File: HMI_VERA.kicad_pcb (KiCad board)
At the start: 2 copper layers, 106 x 74 mm, 34 parts, among them J1 Conn_01x03, J10 Conn_Coaxial, J2 Conn_01x03, J3 Conn_01x03, J4 Conn_01x03, J5 Conn_01x03, J6 Conn_01x03, J7 Conn_01x03, J8 Conn_01x03, J9 DB9_Female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

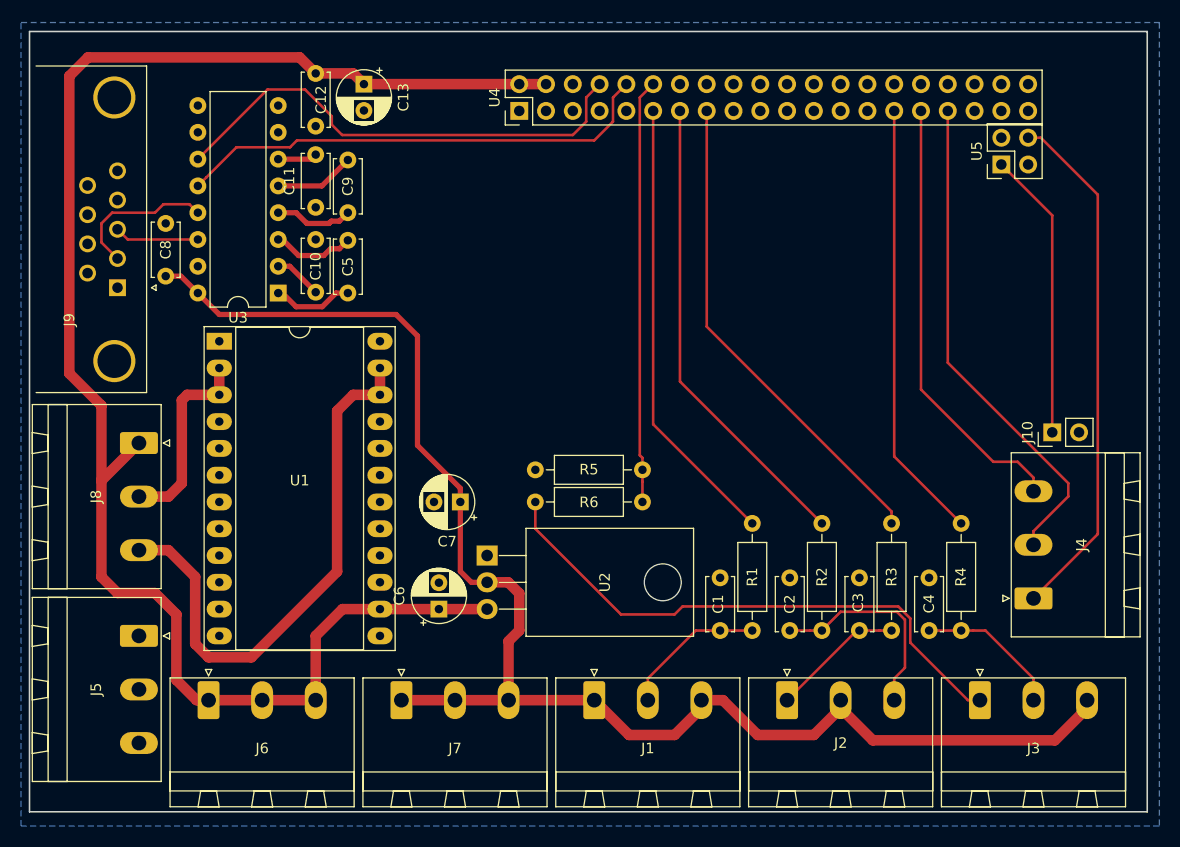
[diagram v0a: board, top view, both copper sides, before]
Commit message: Change to RPi B3+ footprint. PCB currently broken.
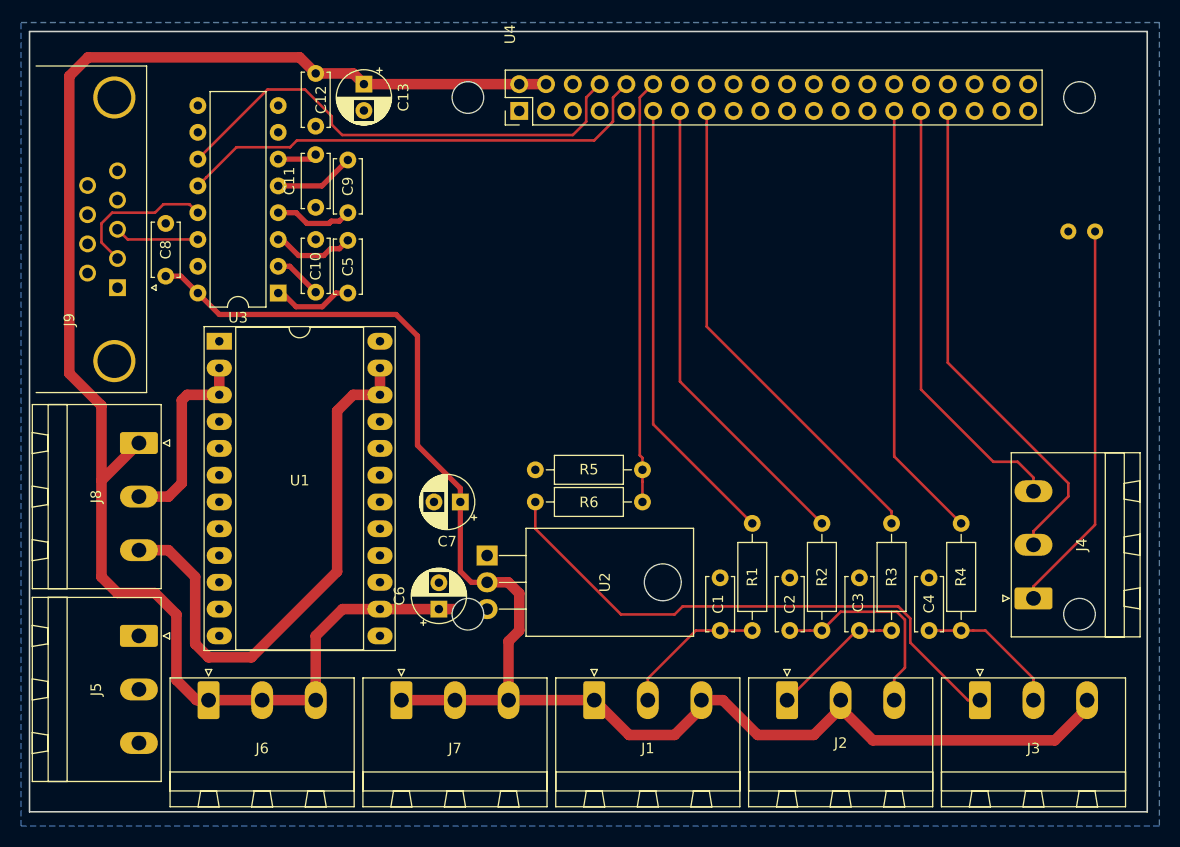
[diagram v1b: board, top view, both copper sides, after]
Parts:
- removed J10: Conn_Coaxial, Connector_PinHeader_2.54mm:PinHeader_1x02_P2.54mm_Vertical
- removed U5: RPI_Zero_RCA_Pinout, Connector_PinHeader_2.54mm:PinHeader_2x02_P2.54mm_Vertical
- U4: value RPI_Zero_Pinout -> RPI_3B+_Pinout_With_RUN; footprint Connector_PinHeader_2.54mm:PinHeader_2x20_P2.54mm_Vertical -> VeraHMI-PCB:RPI_3B+_withRun
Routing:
- net Net-(J10-Pad1): track 27.4 -> 0.00 mm
- net RUN: track 49.7 -> 37.2 mm
